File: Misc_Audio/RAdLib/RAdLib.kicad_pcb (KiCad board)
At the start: 2 copper layers, 129.2 x 56.5 mm, 72 parts, among them J1 Raspberry_Pi_2_3, J2 UART_Header, J3 Power_Output_Header, J4 I2C_Header, J5 AudioJack3, Q1 2N3904, Q201 2N7000, U1 YM3812, U2 YM3014B, U201 74LVC245A, U204 24Cxx, U3 RC4136, U4 LM386, X1 ECS-2100AX-3.579545MHZ

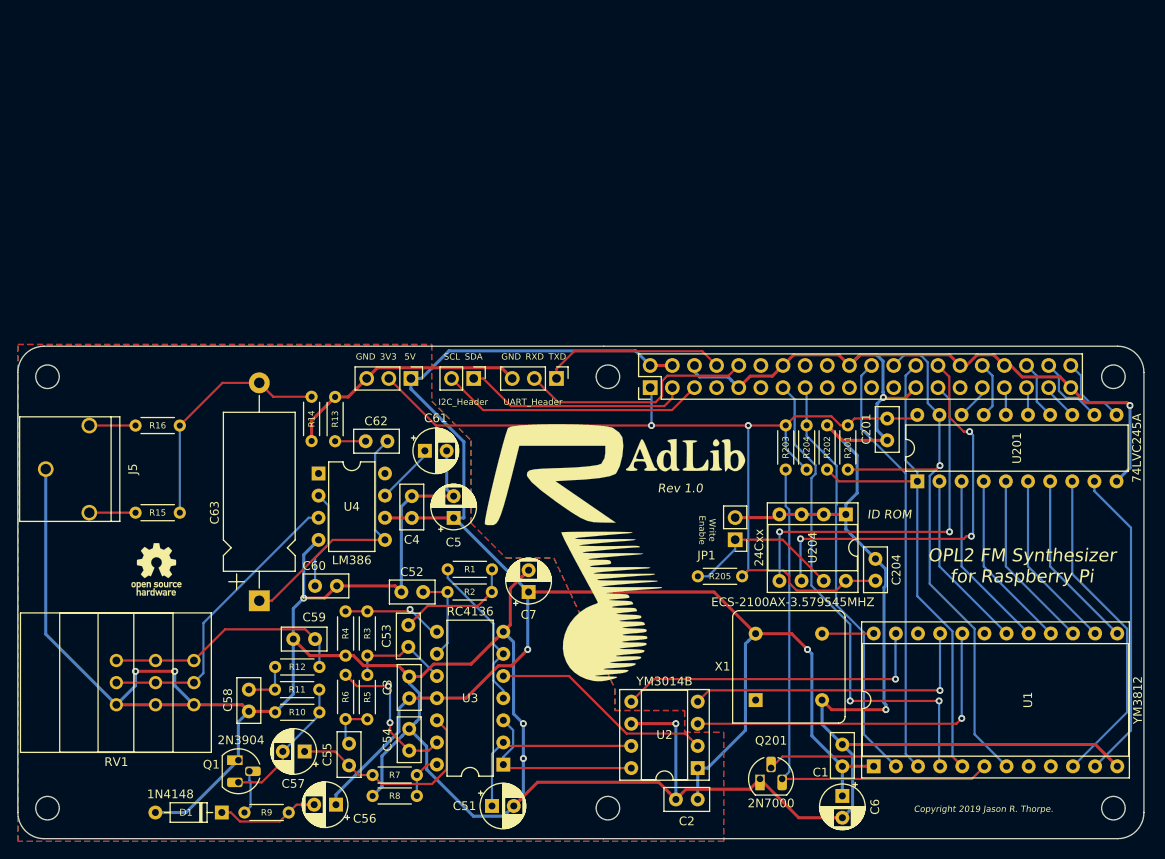
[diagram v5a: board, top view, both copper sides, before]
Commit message: Rework the audio output section as an AC-coupled emitter-follower.
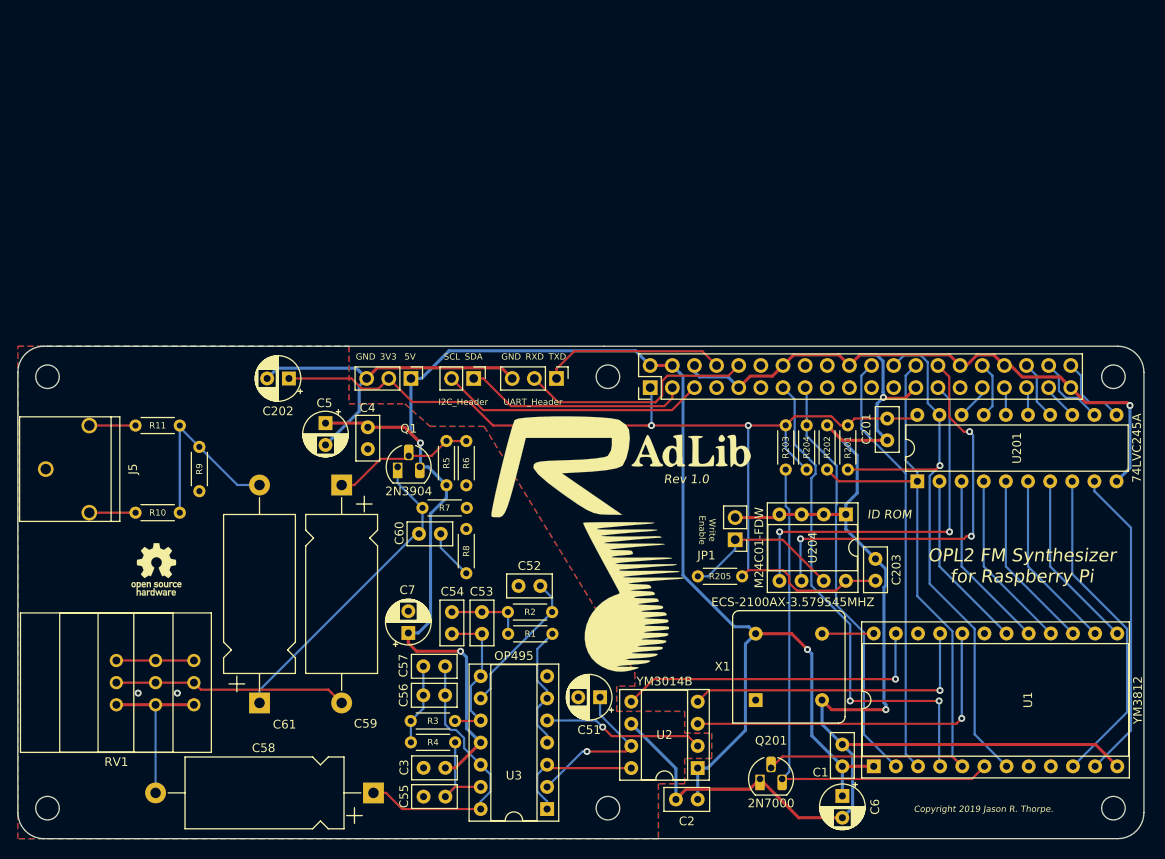
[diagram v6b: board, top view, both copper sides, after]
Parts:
- removed the C61 at (122.7, 99.7)
- removed C62: .047uF, Capacitor_THT:C_Disc_D5.0mm_W2.5mm_P2.50mm
- removed D1: 1N4148, Diode_THT:D_DO-35_SOD27_P7.62mm_Horizontal
- removed the R10 at (110.6, 129.7)
- removed the R11 at (105.5, 127.1)
- removed R12: 8.2K, Resistor_THT:R_Axial_DIN0204_L3.6mm_D1.6mm_P5.08mm_Horizontal
- removed R13: 10R, Resistor_THT:R_Axial_DIN0204_L3.6mm_D1.6mm_P5.08mm_Horizontal
- removed R14: 10K, Resistor_THT:R_Axial_DIN0204_L3.6mm_D1.6mm_P5.08mm_Horizontal
- removed U4: LM386, Package_DIP:DIP-8_W7.62mm
- added C202: 10uF, Capacitor_THT:CP_Radial_D5.0mm_P2.50mm, F.Cu at (107.1, 91.4)
- C52: value 4700pF -> 680pF
- C53: value 4700pF -> 1000pF
- C54: value 4700pF -> 100pF
- C55: value 4700pF -> 470pF
- C56: value 10uF -> 1000pF; footprint Capacitor_THT:CP_Radial_D5.0mm_P2.50mm -> Capacitor_THT:C_Disc_D5.0mm_W2.5mm_P2.50mm
- C57: value 4.7uF -> 100pF; footprint Capacitor_THT:CP_Radial_D5.0mm_P2.50mm -> Capacitor_THT:C_Disc_D5.0mm_W2.5mm_P2.50mm
- C58: value 1000pF -> 220uF; footprint Capacitor_THT:C_Disc_D5.0mm_W2.5mm_P2.50mm -> Capacitor_THT:CP_Axial_L18.0mm_D8.0mm_P25.00mm_Horizontal
- C59: value 270pF -> 220uF; footprint Capacitor_THT:C_Disc_D5.0mm_W2.5mm_P2.50mm -> Capacitor_THT:CP_Axial_L18.0mm_D8.0mm_P25.00mm_Horizontal
- C60: value .1uF -> .047uF
- R1, R2, R9: value 2.2K -> 10K
- R3: value 12K -> 10K
- R5: value 2.2K -> 1K
- R6: value 2.2K -> 2.7K
- R7: value 12K -> 1K
- R8: value 10K -> 10R
- U204: value 24Cxx -> M24C01-FDW
- U3: value RC4136 -> OP495; footprint Package_DIP:DIP-14_W7.62mm -> Package_DIP:DIP-14_W7.62mm_Socket
- moved R9 42.3 mm to (96.8, 99.2), turned to 270 degrees
- moved Q1 38.3 mm to (119.6, 101.5), turned to 0 degrees
- moved R7 31.2 mm to (122.4, 106.2)
- moved R6 30.2 mm to (127.5, 98.6)
- moved R5 28.3 mm to (125.2, 103.7)
- moved R8 27.7 mm to (127.5, 113.8), turned to 90 degrees
- moved C57 18.9 mm to (125.0, 124.4)
- moved C58 18.6 mm to (116.8, 138.9), turned to 180 degrees
- moved C5 18.3 mm to (111.3, 96.5), turned to 270 degrees
- moved C59 17.9 mm to (113.2, 103.6), turned to 270 degrees
- moved C56 17.7 mm to (125.0, 127.8)
- moved C51 17.6 mm to (142.8, 128.0), turned to 180 degrees
- moved R4 16.0 mm to (126.2, 133.2), turned to 180 degrees
- moved C7 14.6 mm to (120.8, 120.6)
- moved C54 14.3 mm to (125.8, 120.7)
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- renumbered C204 to C203, C63 to C61, R15 to R10, R16 to R11
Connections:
- C54 pad 1: Net-(C54-Pad1) -> Net-(C53-Pad1)
- C54 pad 2: GND -> Net-(C53-Pad2)
- C55 pad 1: /FILTER_OUT -> Net-(C55-Pad1)
- C55 pad 2: Net-(C55-Pad2) -> GND
- C56 pad 1: +5V -> /FILTER_OUT
- C57 pad 2: /RC1 -> Net-(C56-Pad2)
- C58 pad 1: /RC2 -> /FILTER_OUT
- C58 pad 2: GND -> /VOL_IN
- C59 pad 1: /RC3 -> /BUFFER_IN
- C59 pad 2: GND -> /VOL_OUT
- C60 pad 1: Net-(C60-Pad1) -> /BUFFER_OUT
- C60 pad 2: GND -> Net-(C60-Pad2)
- C61 pad 1: /AMP_OUT -> /BUFFER_OUT
- Q1 pad 1: GND -> /BUFFER_OUT
- Q1 pad 2: Net-(Q1-Pad2) -> /BUFFER_IN
- Q1 pad 3: /RC1 -> +5V
- R3 pad 1: Net-(C53-Pad1) -> Net-(C56-Pad2)
- R3 pad 2: Net-(R3-Pad2) -> Net-(C53-Pad1)
- R4 pad 1: GND -> Net-(C55-Pad1)
- R4 pad 2: Net-(R3-Pad2) -> Net-(C56-Pad2)
- R5 pad 1: Net-(C55-Pad2) -> +5V
- R5 pad 2: Net-(C53-Pad1) -> /BUFFER_IN
- R6 pad 1: Net-(C54-Pad1) -> /BUFFER_IN
- R6 pad 2: Net-(C55-Pad2) -> GND
- R7 pad 1: /FILTER_OUT -> /BUFFER_OUT
- R7 pad 2: Net-(R7-Pad2) -> GND
- R8 pad 1: GND -> Net-(C60-Pad2)
- R8 pad 2: Net-(R7-Pad2) -> GND
- R9 pad 1: Net-(Q1-Pad2) -> /AUDIO_OUT
- R9 pad 2: Net-(C56-Pad2) -> GND
- RV1 pad 1: /RC3 -> GND (x3)
- RV1 pad 2: /AMP_IN -> /VOL_OUT (x3)
- RV1 pad 3: GND -> /VOL_IN (x3)
- U3 pad 13: Net-(C54-Pad1) -> Net-(C55-Pad1)
- U3 pad 14: Net-(R7-Pad2) -> /FILTER_OUT
- U3 pad 8: Net-(R3-Pad2) -> Net-(C53-Pad1)
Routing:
- net GND: track 512.4 -> 280.0 mm, vias 9 -> 5
- net /BUFFER_OUT: track 0.00 -> 36.2 mm
- net /AMP_IN: track 34.4 -> 0.00 mm
- net /AMP_OUT: track 29.7 -> 0.00 mm
- net /RC3: track 28.2 -> 0.00 mm
- net /VOL_OUT: track 0.00 -> 26.8 mm
- net /VOL_IN: track 0.00 -> 19.0 mm
- net Net-(C54-Pad1): track 17.4 -> 0.00 mm, vias 2 -> 0
- net /BUFFER_IN: track 0.00 -> 16.4 mm
- net /RC1: track 16.1 -> 0.00 mm
- net +3V3: track 110.2 -> 122.6 mm
- net Net-(R3-Pad2): track 11.6 -> 0.00 mm, vias 1 -> 0
- net Net-(C60-Pad1): track 11.5 -> 0.00 mm
- net Net-(C55-Pad1): track 0.00 -> 11.2 mm
- net /FILTER_OUT: track 24.6 -> 32.4 mm
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
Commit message: Use a more generic part # for the ID ROM.
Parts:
- U204: value M24C01-FDW -> 24Cxx
